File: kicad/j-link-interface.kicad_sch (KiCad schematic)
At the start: 5 parts, among them J1 Conn_02x10_Odd_Even, J3 Conn_02x07_Odd_Even, J4 Conn_02x05_Odd_Even, J5 Conn_01x05_Pin, SW1 SW_Push

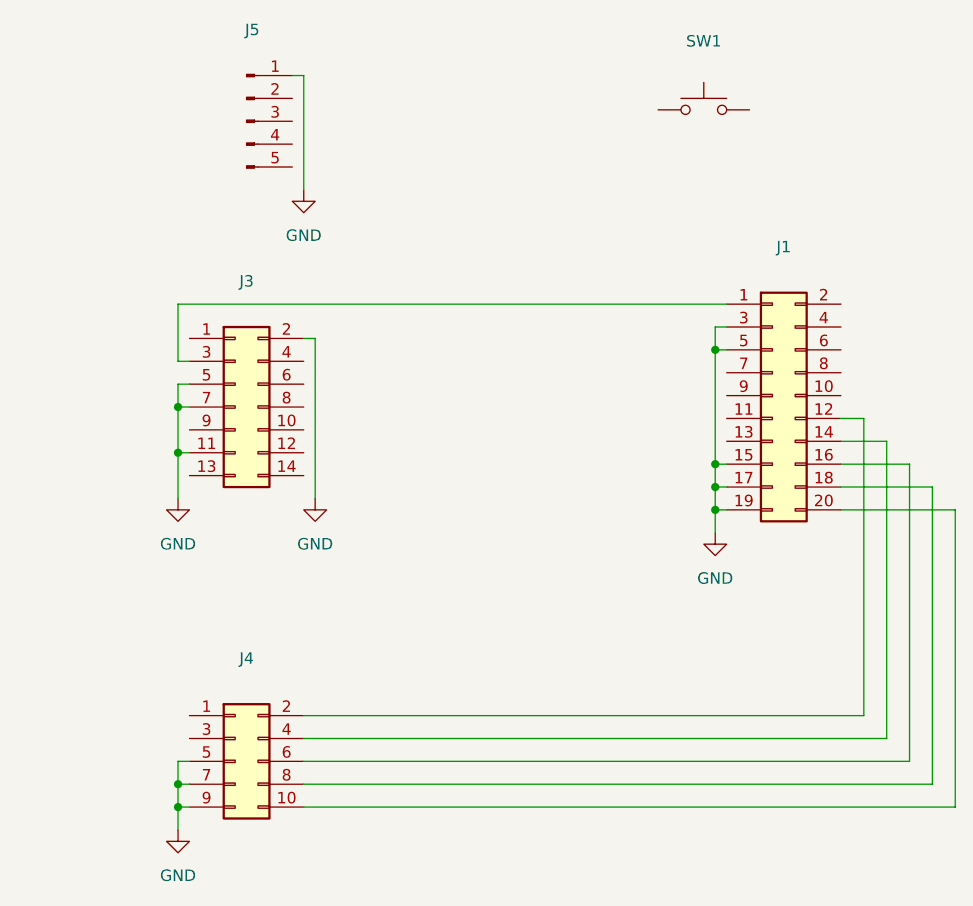
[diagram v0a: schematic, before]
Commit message: Updated reset button. Routed all connections.
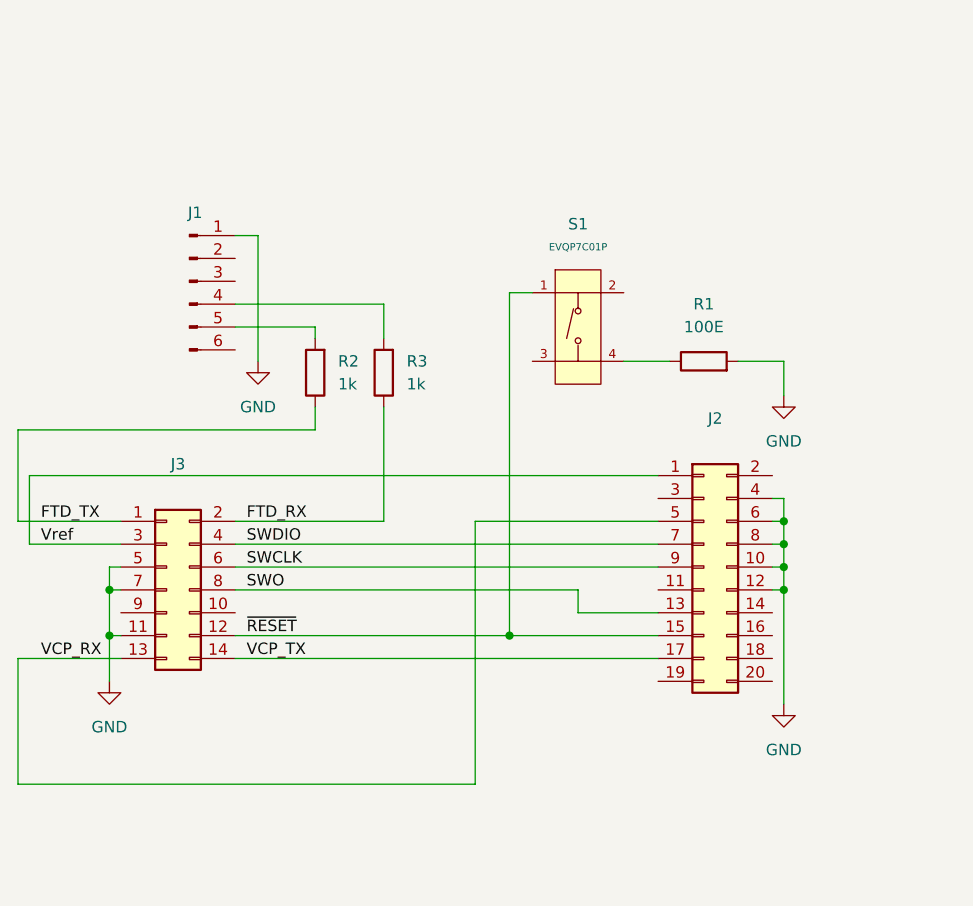
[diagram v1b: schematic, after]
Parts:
- removed J4: Conn_02x05_Odd_Even, symbol Connector_Generic:Conn_02x05_Odd_Even
- removed SW1: SW_Push, symbol Switch:SW_Push
- added R1: 100E, Resistor_SMD:R_0201_0603Metric, symbol Device:R
- added R2, R3: 1k, Resistor_SMD:R_0201_0603Metric, symbol Device:R
- added S1: EVQP7C01P, local_library:SW_EVQ-P7C01P, symbol PCM_JLCPCB-Connectors_Buttons:Tactile Button, 160gf, 12V, 50mA, 5.1mm
- J1: renamed from J5; footprint (none) -> Connector_PinHeader_2.54mm:PinHeader_1x06_P2.54mm_Vertical; symbol Connector:Conn_01x05_Pin -> Connector:Conn_01x06_Pin; LCSC (none) -> C3347142; MF (none) -> TE Connectivity; MP (none) -> 5-146280-6
- J2: renamed from J1; value Conn_02x10_Odd_Even -> SSW-110-02-G-D-RA-N; footprint (none) -> local_library:SAMTEC_SSW-110-02-G-D-RA-N; LCSC (none) -> C6236423; MF (none) -> Samtec; MP (none) -> SSW-110-02-G-D-RA-N
- J3: value Conn_02x07_Odd_Even -> FTSH-107-01-X-DV-K; footprint (none) -> local_library:SAMTEC_FTSH-107-01-X-DV-K; LCSC (none) -> C5307809; MF (none) -> Samtec; MP (none) -> FTSH-107-01-X-DV-K
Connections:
- net GND: now also J2.10 (Pin_10), J2.12 (Pin_12), J2.4 (Pin_4), J2.6 (Pin_6), J2.8 (Pin_8), R1.2; no longer J2.15 (Pin_15), J2.17 (Pin_17), J2.19 (Pin_19), J2.3 (Pin_3), J2.5 (Pin_5), J3.2 (Pin_2)
- net FTD_TX: now reaches J3.1 (Pin_1)
- net FTD_TX: now also R2.1
- net ~{RESET}: now reaches J3.12 (Pin_12)
- net ~{RESET}: now also J2.15 (Pin_15), S1.1 (A)
- net VCP_RX: now reaches J3.13 (Pin_13)
- net VCP_RX: now also J2.5 (Pin_5)
- net VCP_TX: now reaches J3.14 (Pin_14)
- net VCP_TX: now also J2.17 (Pin_17)
- net Vref: now reaches J2.1 (Pin_1), J3.3 (Pin_3)
- net SWDIO: now reaches J3.4 (Pin_4)
- net SWDIO: now also J2.7 (Pin_7)
- net SWCLK: now reaches J3.6 (Pin_6)
- net SWCLK: now also J2.9 (Pin_9)
- net SWO: now reaches J3.8 (Pin_8)
- net SWO: now also J2.13 (Pin_13)
- net at J1.4 (Pin_4): now also R3.2
- net at J1.5 (Pin_5): now also R2.2
- new net: R1.1, S1.4 (D)
- new net FTD_RX: J3.2 (Pin_2), R3.1
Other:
- company: (none) -> NX Solutions
- title: (none) -> J-Link Interface
- moved on the sheet: J2, J3
